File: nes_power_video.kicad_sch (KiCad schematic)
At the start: 23 parts, among them J2 Audio, J3 Video, J4 Conn_01x05, J5 RGB conn feed, Q1 KSA1015, U1 TPS2553DBV

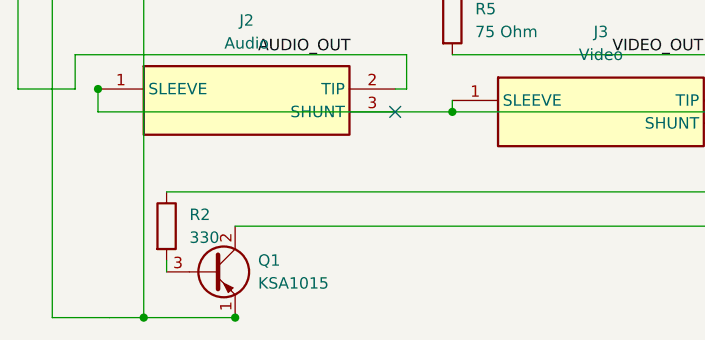
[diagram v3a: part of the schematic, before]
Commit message: Switch Q1 to the 2SA733: in production, drop-in pinout, better part
Both previous candidates are end of life, so Q1 was specified on borrowed
time either way. The 2SA733 is in current production from UTC, shares the
E-C-B pin order exactly - collector in the middle - so it drops into the
existing TO-92 footprint with no layout change, and it is a better part
for a video buffer than what it replaces:

  fT   190 MHz typ   vs the 2SA1015's 80 MHz
  Cob  2-3 pF
  PC   750 mW (TO-92)
  VCEO -50 V, IC -150 mA, VEBO -5 V   unchanged, so R2 still guards B-E

Rank P is hFE 200-400, matching the ~46 uA base current measured on the
bench at ~9.3 mA emitter, so the bias point does not move and no other
component changes. Buy UTC 2SA733L-P-T92-B from LCSC (C5310429, $0.035):
DigiKey's Renesas 2SA733 shows Active with 81k stock but ships from
Rochester at $1.90, the same last-time-buy channel the KSA1015 was stuck
in. Pinout confirmed from UTC's ordering table, not from a drawing.

The README's 2N3906 warning was accurate but read as if the part were
electrically unsuitable, which it is not. Rewritten to say what actually
bites: the 2N3906 is E-B-C against the 2SA733's E-C-B, so it puts BASE in
the middle pin where this board wants COLLECTOR. Rotating it gives C-B-E
and base is still in the middle, so no orientation fixes it - it needs two
leads crossed. On a v3 layout the pin order is free and the 2N3906 becomes
a good choice; on this board it is not.

Schematic keeps the Transistor_BJT:2SA1015 symbol - same pinout family,
and swapping it would only churn the cached lib_symbols.

Verified: ERC 0 violations, check_nets.py all invariants pass, DRC
violation set identical to the previous commit, both new links resolve
(LCSC 200, UTC datasheet 200 application/pdf). Silkscreen now reads
2SA733; no copper touched.

Co-Authored-By: Claude Opus 5 <noreply@anthropic.com>
Claude-Session: https://claude.ai/code/session_01SFPsiQ6ZtUgKSkh2NG4xCg
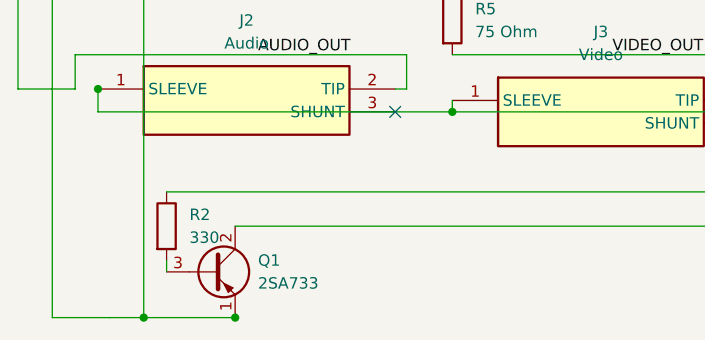
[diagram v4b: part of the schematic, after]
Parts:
- Q1: value KSA1015 -> 2SA733; LCSC (none) -> C5310429; MPN KSA1015GRTA -> 2SA733L-P-T92-B; Manufacturer onsemi -> UTC (Unisonic); Spec PNP TO-92, E-C-B pinout, any hFE grade. END OF LIFE both wa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 -> PNP TO-92, pin order E-C-B (collector in the middle) - data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; Supplier Link https://www.digikey.com/en/products/detail/rochester-electr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 -> https://www.lcsc.com/product-detail/C5310429.html
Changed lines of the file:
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@@
 			)
 		)
-		(property "Value" "KSA1015"
+		(property "Value" "2SA733"
 			(at 40.64 190.4999 0)
 			(show_name no)
@@
 			)
 		)
-		(property "Datasheet" "https://www.onsemi.com/download/data-sheet/pdf/ksa1015-d.pdf"
+		(property "Datasheet" "https://www.unisonic.com.tw/uploadfiles/836/part_no_pdf/2SA733.pdf"
 			(at 35.56 189.23 0)
 			(hide yes)
@@
 			)
 		)
-		(property "Manufacturer" "onsemi"
+		(property "Manufacturer" "UTC (Unisonic)"
 			(at 35.56 189.23 0)
 			(hide yes)
@@
 			)
 		)
-		(property "MPN" "KSA1015GRTA"
+		(property "MPN" "2SA733L-P-T92-B"
 			(at 35.56 189.23 0)
 			(hide yes)
@@
 			)
 		)
-		(property "Spec" "PNP TO-92, E-C-B pinout, any hFE grade. END OF LIFE both ways: onsemi KSA1015 is obsolete, stocked only as KSA1015GRTA-ON through Rochester; MCC 2SA1015-GR-AP is on Mouser but flagged End of Life. Needs a live replacement for v3."
+		(property "Spec" "PNP TO-92, pin order E-C-B (collector in the middle) - datasheet ordering table, not a drawing. Rank P = hFE 200-400, matching the ~46 uA base current measured at ~9.3 mA emitter. VCEO -50 V, IC -150 mA, VEBO -5 V (same as the 2SA1015 it replaces, so R2 still guards the B-E junction), fT 190 MHz typ, Cob 2-3 pF. Schematic reuses the Transistor_BJT:2SA1015 symbol - same pinout family."
 			(at 35.56 189.23 0)
 			(hide yes)
@@
 			)
 		)
-		(property "Supplier Link" "https://www.digikey.com/en/products/detail/rochester-electronics-llc/KSA1015GRTA-ON/12643065"
+		(property "Supplier Link" "https://www.lcsc.com/product-detail/C5310429.html"
 			(at 35.56 189.23 0)
 			(hide yes)
+			(show_name no)
+			(do_not_autoplace no)
+			(effects
+				(font
+					(size 1.27 1.27)
+				)
+			)
+		)
+		(property "LCSC" "C5310429"
+			(at 35.56 189.23 0)
+			(hide yes)
